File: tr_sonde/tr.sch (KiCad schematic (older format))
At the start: 83 parts, among them J1 SMA, J2 SMA, J3 SMA, K1 TR, K2 HV_MON, K3 VINHDR, Q1 PBSS4250X, Q2 MMBT2222A, Q3 STD2NK90ZT4, Q4 STD2NK90ZT4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

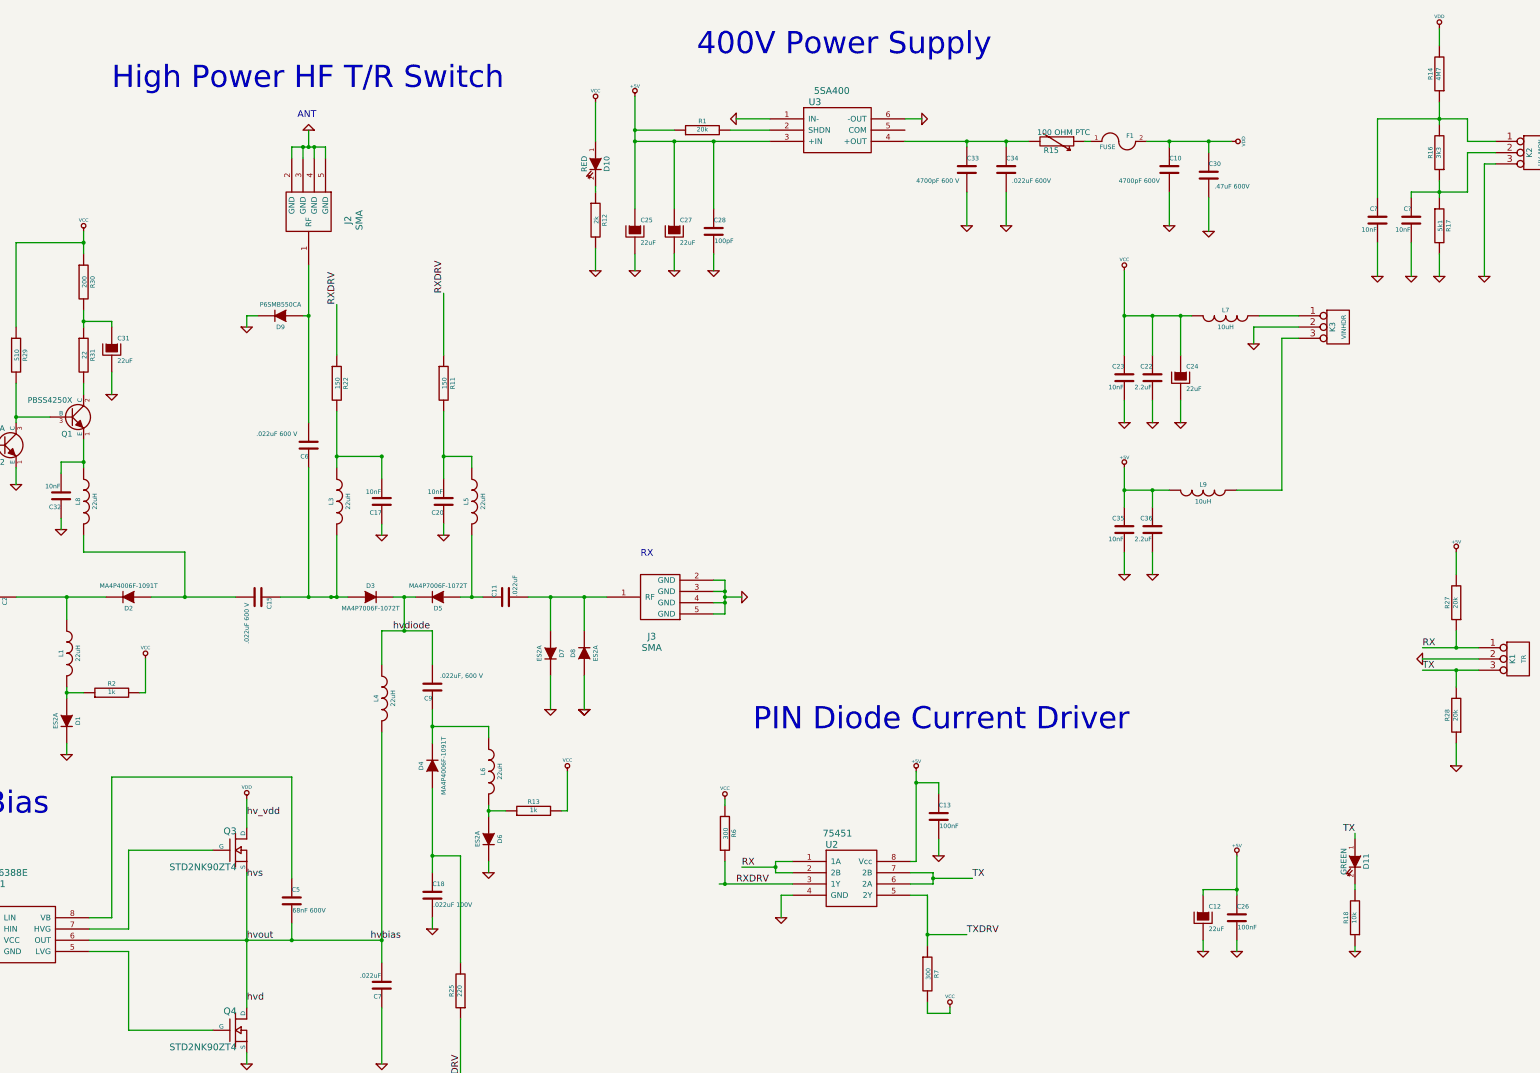
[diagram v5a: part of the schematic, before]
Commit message: polishing agc, tr, and driver amp for next revisions. moved all bottom layer signal traces to top layer on driver amp
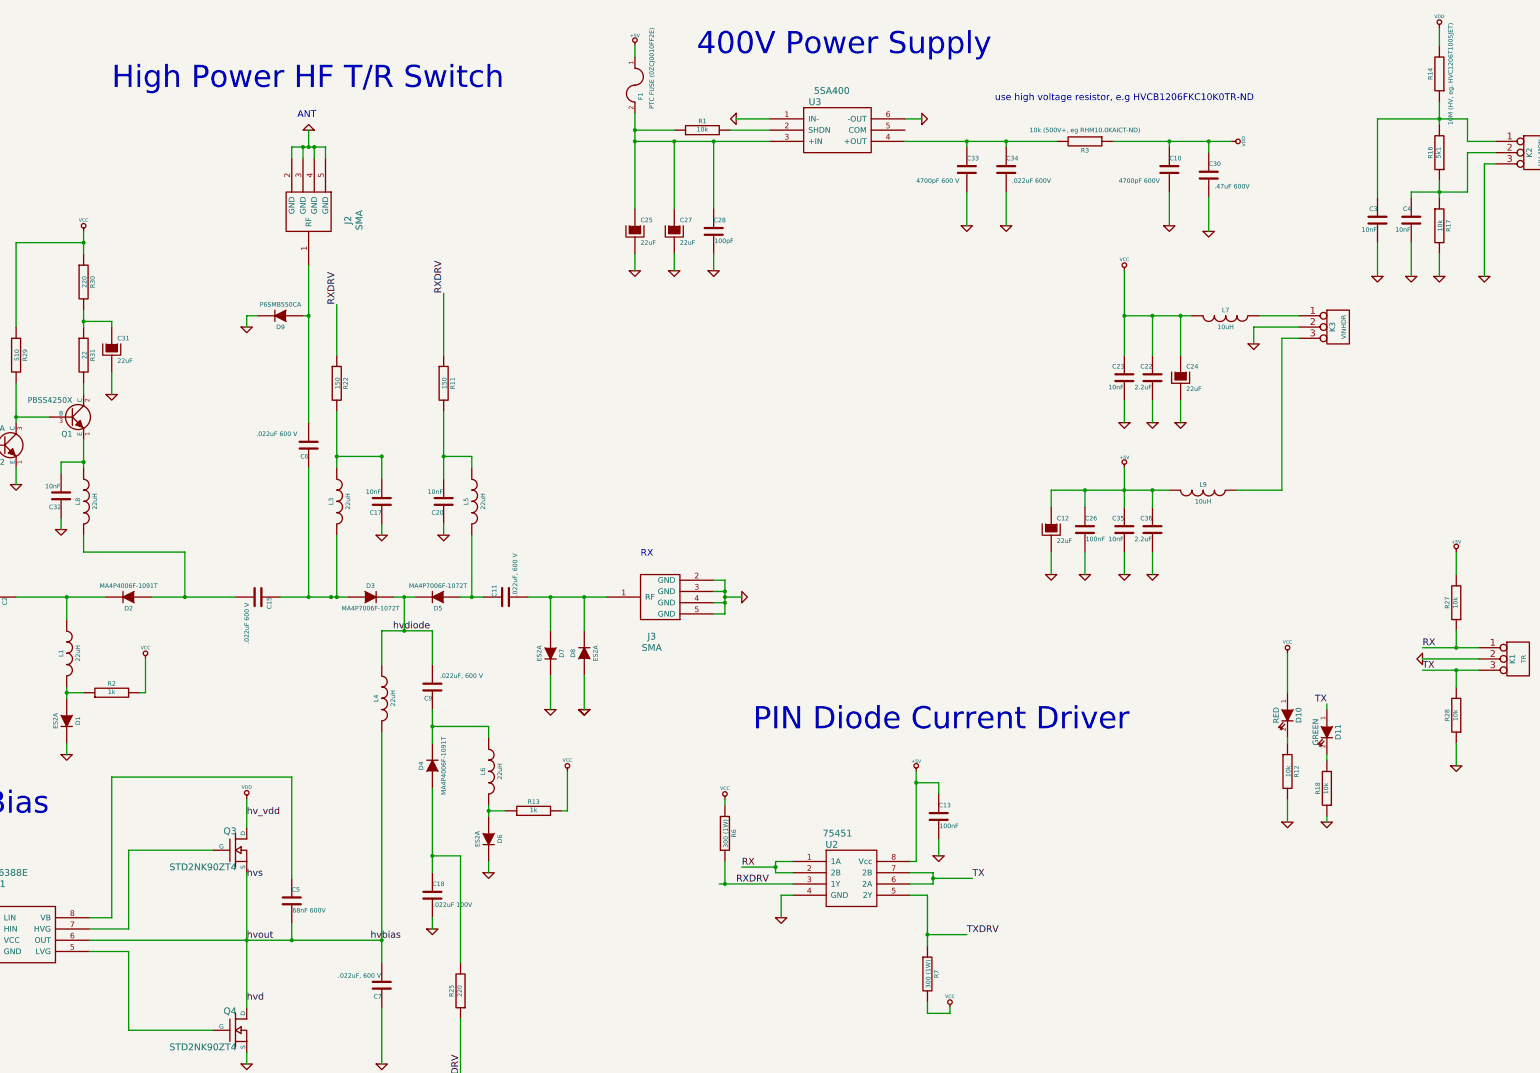
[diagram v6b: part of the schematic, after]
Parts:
- removed R15: 100 OHM PTC, smd_capacitors:c_1210, symbol RVAR
- added R3: 10k (500V+, eg RHM10.0KAICT-ND), symbol R
- C11, C7: value .022uF -> .022uF, 600 V
- F1: value FUSE -> PTC FUSE (0ZCJ0010FF2E)
- R1, R27, R28: value 20k -> 10k
- R12: value 2k -> 10k
- R14: value 4M7 -> 10M (HV, eg. HVC1206T1005JET); footprint smd_capacitors:c_0805 -> smd_capacitors:c_1206
- R16: value 3k3 -> 5k1
- R17: value 5k1 -> 10k
- R30: value 200 -> 220
- R6, R7: value 300 -> 300 (1W)
- gave numbers to parts that had none: 2
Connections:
- net +5V: now also F1.1; no longer C25.1, C27.1, C28.1, R1.1, U3.3 (+IN)
- net VDD: now also R3.1; no longer F1.2
- net at C33.1, C34.1, U3.4 (+OUT): now also R3.2
- new net: C25.1, C27.1, C28.1, F1.2, R1.1, U3.3 (+IN)
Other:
- note added: "use high voltage resistor, e.g HVCB1206FKC10K0TR-ND"
- moved on the sheet: C12, C26, D10, D11, F1, R12, R18

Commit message: added notes to tr
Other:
- note added: "trip at 300 mA, nominal 200 mA"
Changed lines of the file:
@@
 Wire Wire Line
 	12100 5400 12100 5600
+Text Notes 7850 600  0    60   ~ 0
+trip at 300 mA, nominal 200 mA
 $EndSCHEMATC

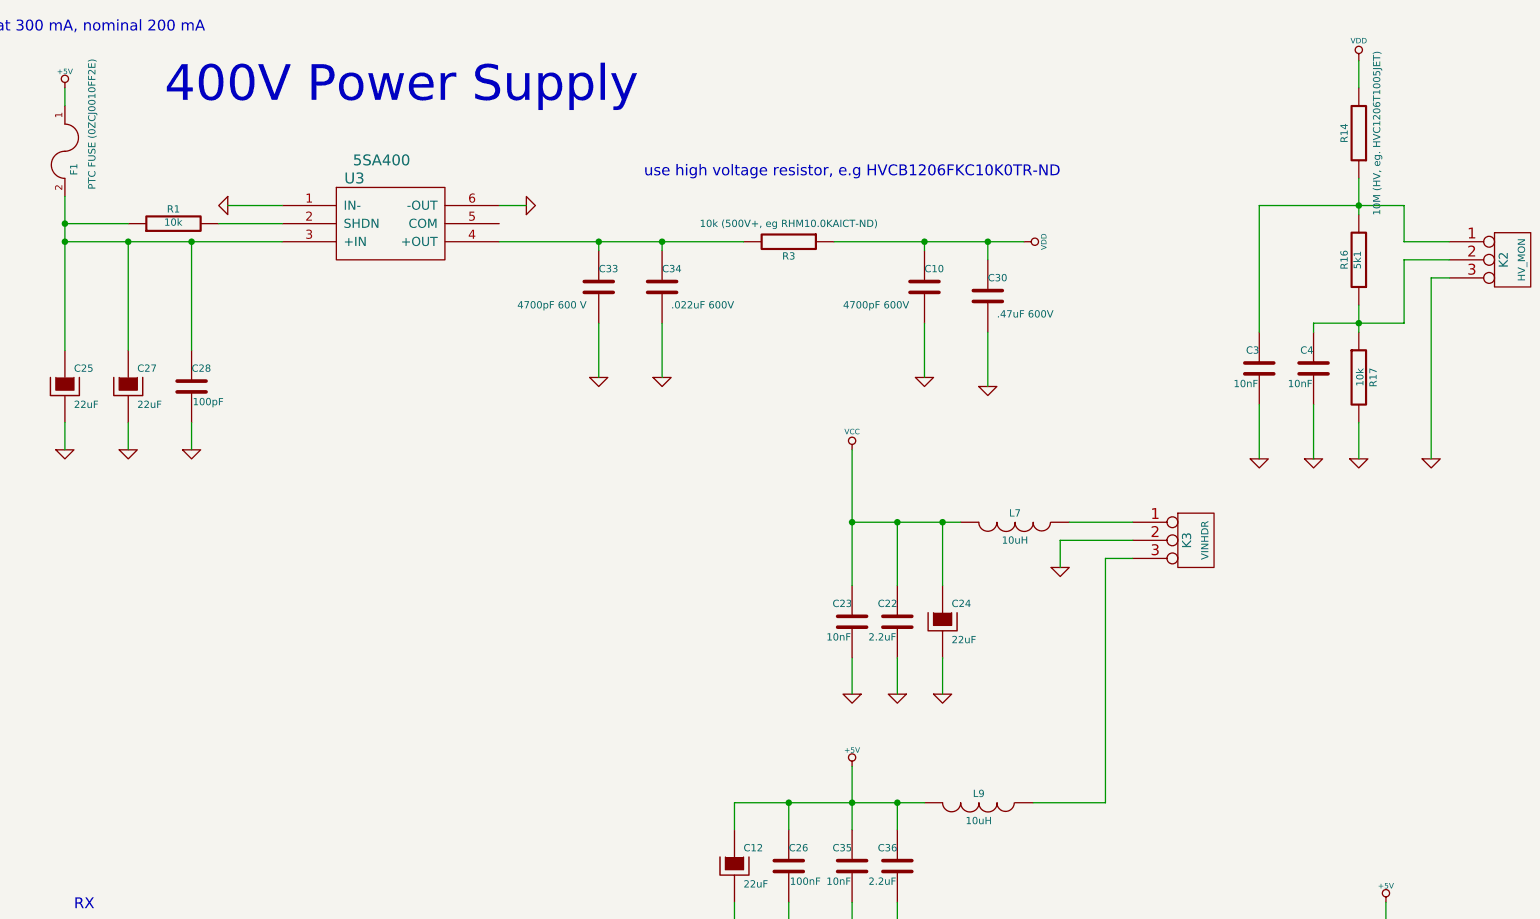
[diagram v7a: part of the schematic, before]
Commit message: started on t/r with enclosure, migrated distro to 15v
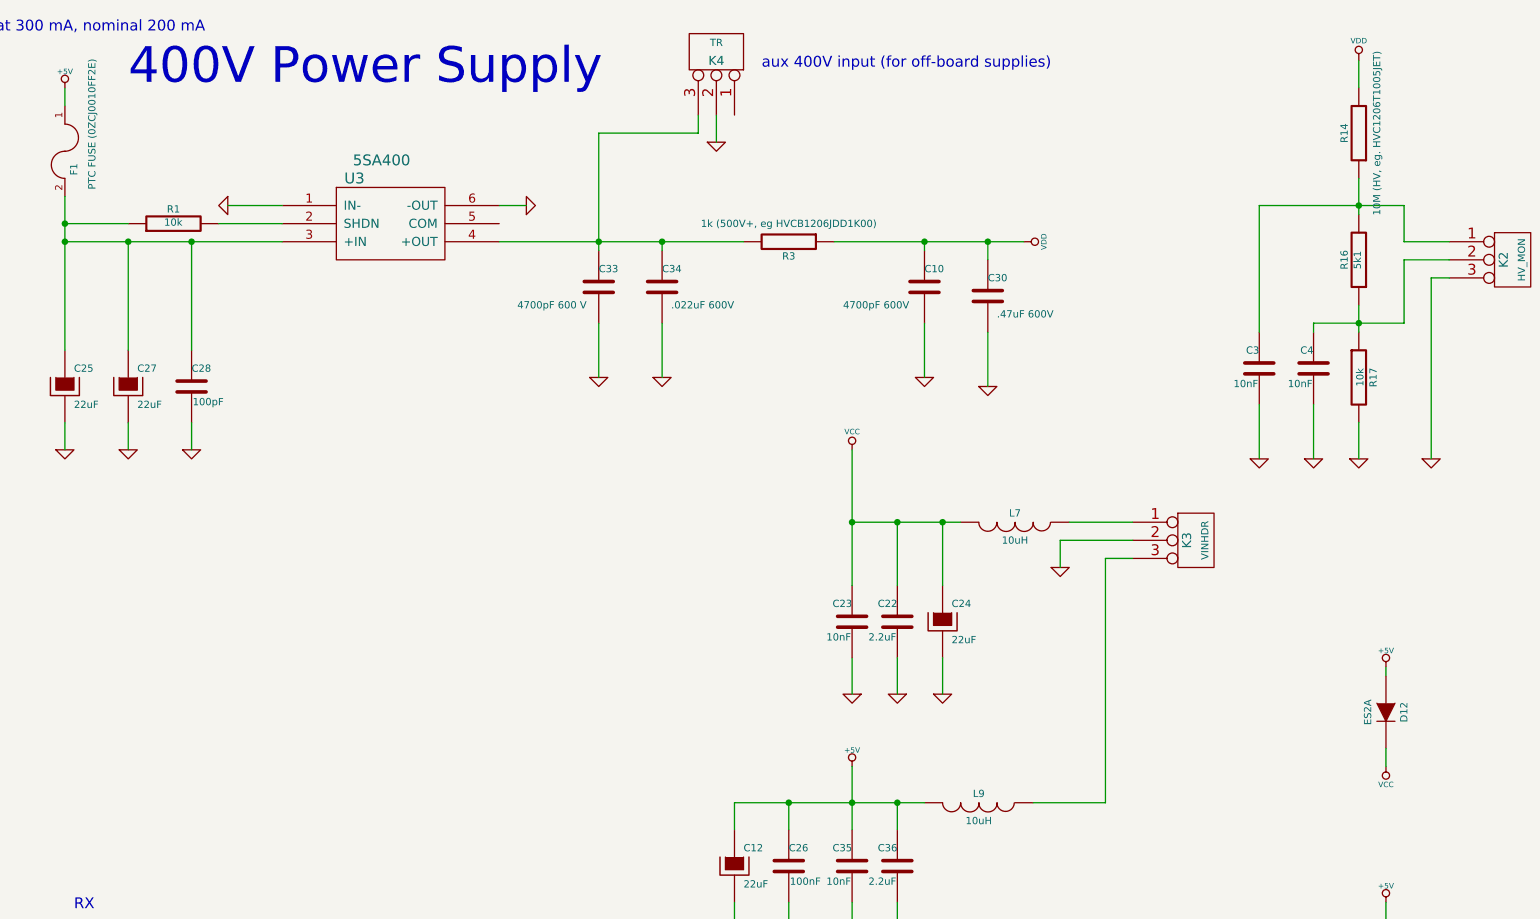
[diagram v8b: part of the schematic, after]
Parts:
- added D12: ES2A, smb_diode:SMB_DO2144AA, symbol DIODE
- added K4: TR, Connect:PINHEAD1-3, symbol CONN_3
- C33: footprint Capacitors_SMD:c_1206 -> SMD_Packages:SMD-1210
- C34: footprint smd_capacitors:c_1206 -> SMD_Packages:SMD-1210
- C5, R11, R22, R25, R30: footprint smd_capacitors:c_0805 -> SMD_Packages:SMD-1210
- D2, D4: footprint smb_diode:SMB_DO2144AA -> Diodes_SMD:Diode-SMB_Handsoldering
- Q1: footprint SMD_Packages:SOT23EBC -> Transistors_SMD:sot89
- Q2: footprint Transistors_SMD:sot89 -> SMD_Packages:SOT23EBC
- R14: footprint smd_capacitors:c_1206 -> SMD_Packages:SM1210
- R3: value 10k (500V+, eg RHM10.0KAICT-ND) -> 1k (500V+, eg HVCB1206JDD1K00); footprint (none) -> SMD_Packages:SM1210
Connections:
- net +5V: now also D12.1 (A)
- net GND: now also K4.2 (PM)
- net VCC: now also D12.2 (K)
- net at C33.1, C34.1, R3.2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: now also K4.3 (P3)
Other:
- note added: "aux 400V input (for off-board supplies)"
- note removed: "use high voltage resistor, e.g HVCB1206FKC10K0TR-ND"
